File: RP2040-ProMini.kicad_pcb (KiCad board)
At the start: 4 copper layers, 17.8 x 33 mm, 33 parts, among them J1 CONN_L, J2 CONN_U, J3 CONN_R2, J4 CONN_R, Q1 AO3400A, U1 W25Q128JVS, U2 RP2040, U3 MIC5205-3.3YM5, Y1 12MHz

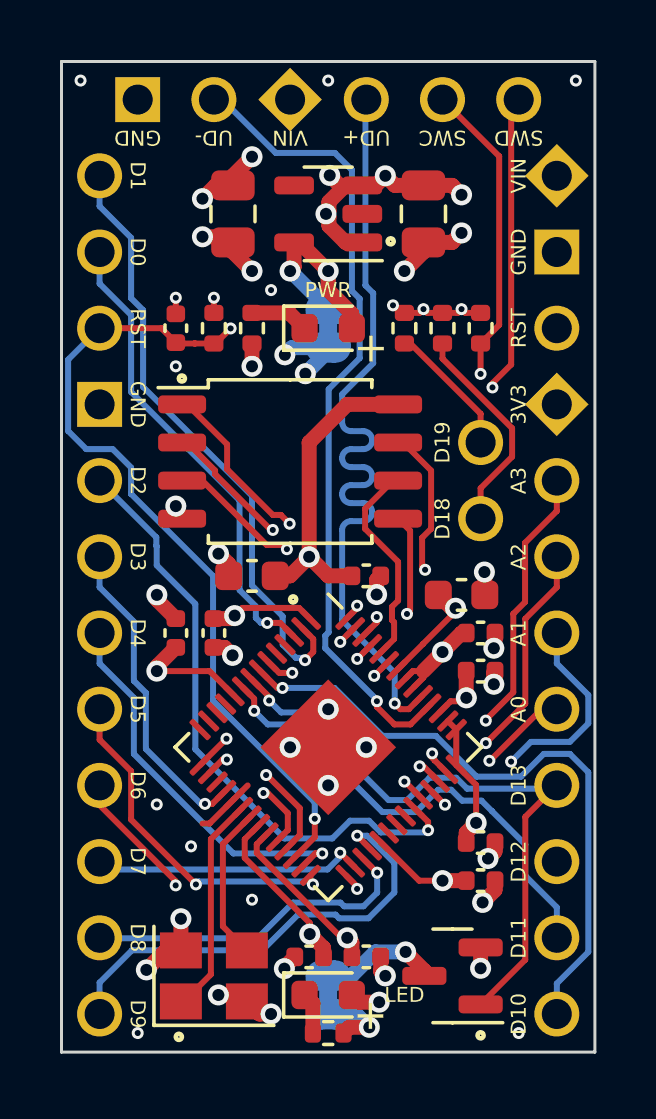
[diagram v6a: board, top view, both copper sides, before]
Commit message: Optimized routing a lot.
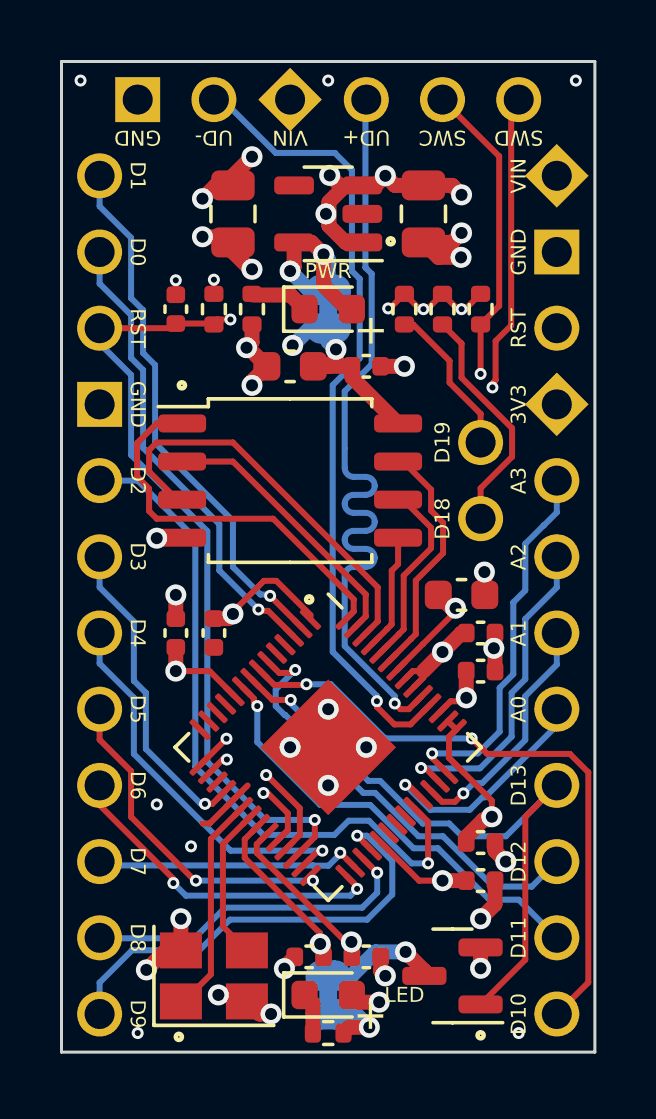
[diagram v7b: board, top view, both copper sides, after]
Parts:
- moved C1 7.10 mm to (154.9, 104.1)
- moved C2 6.98 mm to (157.5, 104.1)
- moved C13 0.64 mm to (151.1, 102.2)
- moved D2 0.64 mm to (156.2, 102.2)
- moved JP2 0.64 mm to (156.2, 102.2)
- moved R2 0.64 mm to (161.3, 102.2)
- moved R3 0.64 mm to (158.8, 102.2)
- moved R4 0.64 mm to (160.0, 102.2)
- moved R5 0.64 mm to (152.4, 102.2)
- moved R6 0.64 mm to (153.7, 102.2)
- moved U1 0.64 mm to (154.9, 108.0)
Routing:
- net +3V3: track 58.2 -> 40.2 mm, vias 16 -> 15
- net QSPI_SD2: track 9.56 -> 13.8 mm, vias 2 -> 0
- net QSPI_SD0: track 7.11 -> 3.93 mm, vias 2 -> 0
- net D18_SDA: track 24.2 -> 21.2 mm
- net SWD: track 34.8 -> 32.0 mm
- net SWCLK: track 35.0 -> 32.2 mm
- net QSPI_SS: track 10.3 -> 13.0 mm, vias 2 -> 0
- net D19_SCL: track 23.2 -> 20.5 mm
- net D2: track 20.7 -> 23.2 mm
- net D1_TX: track 20.5 -> 18.0 mm
- net QSPI_SD3: track 10.4 -> 8.14 mm, vias 2 -> 0
- net D15_A1: track 10.0 -> 8.16 mm, vias 2 -> 1
- net GND: track 21.9 -> 23.6 mm, vias 37 -> 32
- net D11_MOSI: track 16.0 -> 14.7 mm
- net D12_MISO: track 13.5 -> 14.8 mm
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
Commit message: Optimized routing even more.
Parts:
- moved R3 1.28 mm to (160.0, 102.4)
- moved R4 1.28 mm to (158.8, 102.4)
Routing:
- net GND: track 23.6 -> 27.9 mm, vias 32 -> 47
- net D18_SDA: track 21.2 -> 23.1 mm
- net +3V3: track 40.2 -> 41.7 mm, vias 15 -> 16
- net D7: track 8.95 -> 10.4 mm
- net D6: track 11.3 -> 9.96 mm, vias 2 -> 1
- net D5: track 11.2 -> 10.2 mm, vias 2 -> 1
- net D19_SCL: track 20.5 -> 21.2 mm
- net +1V1: track 24.2 -> 24.8 mm
- net D8: track 11.2 -> 11.8 mm
